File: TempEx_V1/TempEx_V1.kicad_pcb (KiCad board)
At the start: 4 copper layers, 50 x 40 mm, 29 parts, among them J1 Conn_01x02, J2 Conn_01x10, J3 Conn_01x02, J4 Conn_01x02, J5 Conn_01x02, U1 MAX31865xTP, U2 MAX31865xTP, U3 MAX31865xTP, U4 MAX31865xTP

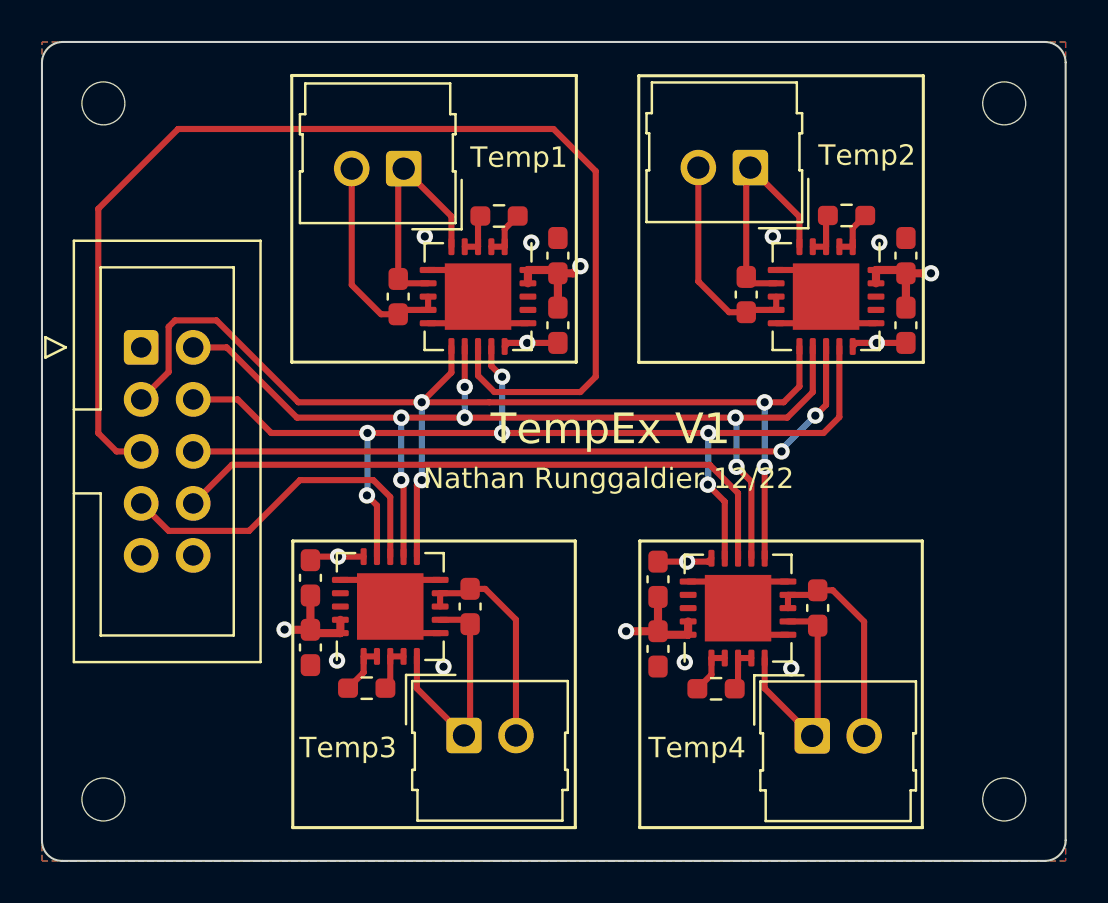
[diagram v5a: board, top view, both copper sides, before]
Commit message: Layer change + 4 pin setup + stitching
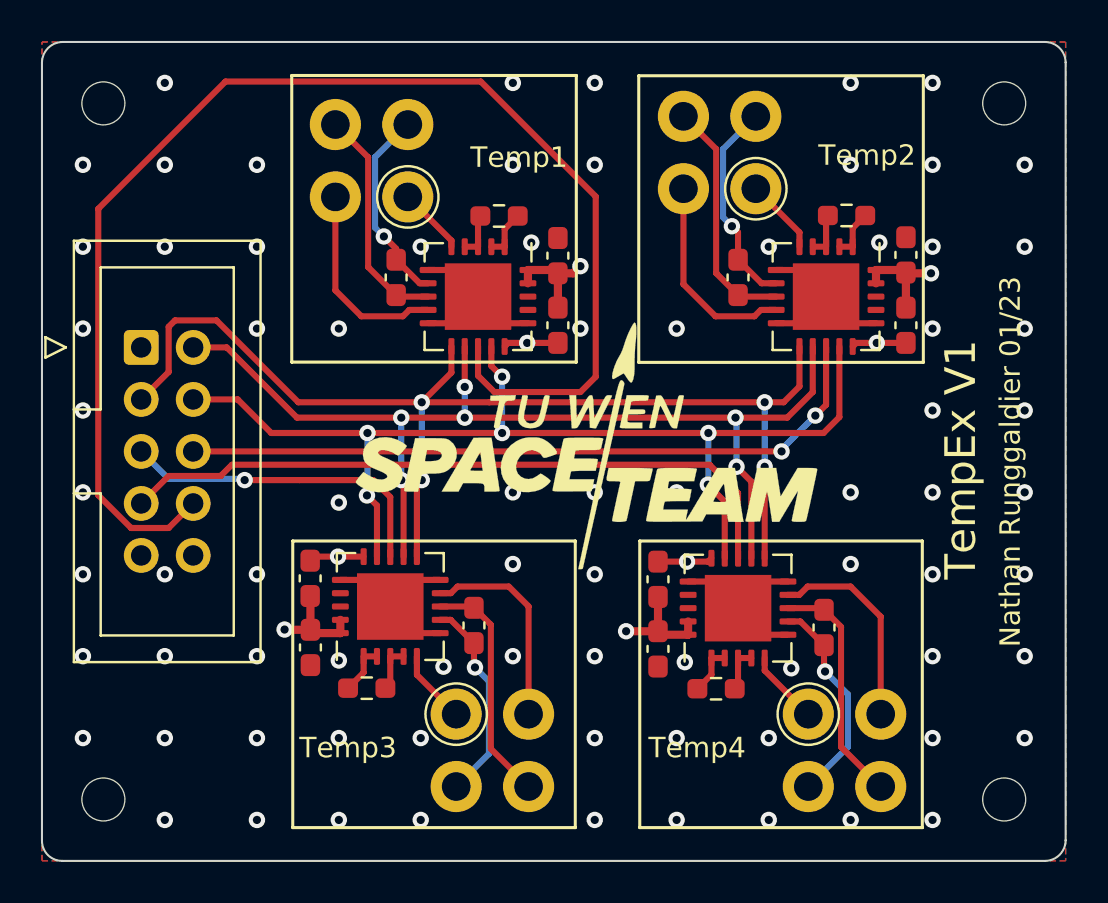
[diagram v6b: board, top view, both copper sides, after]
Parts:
- added G1: SpaceTeam_LOGO, TXV_Library_Footprints:ST_Logo_new, F.Cu at (126.6, 124.7)
- J1, J3, J4, J5: value Conn_01x02 -> Conn_01x04; footprint Connector_Molex:Molex_SL_171971-0002_1x02_P2.54mm_Vertical -> TXV_Library_Footprints:TE_M12_4_Pin_PCB
- moved C6 25.5 mm to (134.0, 116.5), turned to -90 degrees
- moved C3 24.9 mm to (117.3, 116.5), turned to -90 degrees
- moved C9 16.5 mm to (121.1, 133.5), turned to 90 degrees
- moved C10 8.04 mm to (142.2, 115.4), turned to 90 degrees
- moved C11 7.93 mm to (113.1, 131.2)
- moved J5 1.73 mm to (139.2, 139.6), turned to 90 degrees
- moved J3 1.67 mm to (133.1, 110.4), turned to -90 degrees
- moved J1 1.62 mm to (116.1, 110.8), turned to -90 degrees
- moved J4 1.57 mm to (122.0, 139.6), turned to 90 degrees
- moved C12 1.00 mm to (138.2, 133.6)
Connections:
- net /Temperature/SPI_CLK renamed /SPI_CLK
- net /Temperature/SPI_MISO renamed /SPI_MISO
- net /Temperature/SPI_MOSI renamed /SPI_MOSI
- net /Temperature/SPI_NSS2 renamed /SPI_NSS2
- C10 pad 1: Net-(C10-Pad1) -> +3V3
- C10 pad 2: Net-(C10-Pad2) -> GND
- C11 pad 1: Net-(C11-Pad1) -> +3V3
- C11 pad 2: Net-(C11-Pad2) -> GND
- C3 pad 1: +3V3 -> Net-(C3-Pad1)
- C3 pad 2: GND -> Net-(C3-Pad2)
- C6 pad 1: +3V3 -> Net-(C6-Pad1)
- C6 pad 2: GND -> Net-(C6-Pad2)
- J1 pad 1: Net-(C9-Pad1) -> Net-(J1-Pad1)
- J1 pad 2: Net-(C9-Pad2) -> Net-(C3-Pad1)
- J2 pad 5: /Temperature/SPI_NSS1 -> /SPI_NSS1
- J2 pad 7: /Temperature/SPI_NSS3 -> /SPI_NSS3
- J2 pad 8: /Temperature/SPI_NSS4 -> /SPI_NSS4
- J3 pad 1: Net-(C10-Pad1) -> Net-(J3-Pad1)
- J3 pad 2: Net-(C10-Pad2) -> Net-(C6-Pad1)
- J4 pad 1: Net-(C11-Pad1) -> Net-(J4-Pad1)
- J4 pad 2: Net-(C11-Pad2) -> Net-(C9-Pad1)
- J5 pad 1: Net-(C12-Pad1) -> Net-(J5-Pad1)
- J5 pad 2: Net-(C12-Pad2) -> Net-(C12-Pad1)
- U1 pad 13: /Temperature/SPI_NSS1 -> /SPI_NSS4
- U1 pad 5: Net-(C9-Pad1) -> Net-(J1-Pad1)
- U1 pad 7: Net-(C9-Pad1) -> Net-(C3-Pad1)
- U1 pad 8: Net-(C9-Pad2) -> Net-(C3-Pad2)
- U1 pad 9: Net-(C9-Pad2) -> Net-(J1-Pad4)
- U2 pad 5: Net-(C10-Pad1) -> Net-(J3-Pad1)
- U2 pad 7: Net-(C10-Pad1) -> Net-(C6-Pad1)
- U2 pad 8: Net-(C10-Pad2) -> Net-(C6-Pad2)
- U2 pad 9: Net-(C10-Pad2) -> Net-(J3-Pad4)
- U3 pad 13: /Temperature/SPI_NSS3 -> /SPI_NSS1
- U3 pad 5: Net-(C11-Pad1) -> Net-(J4-Pad1)
- U3 pad 7: Net-(C11-Pad1) -> Net-(C9-Pad1)
- U3 pad 8: Net-(C11-Pad2) -> Net-(C9-Pad2)
- U3 pad 9: Net-(C11-Pad2) -> Net-(J4-Pad4)
- U4 pad 13: /Temperature/SPI_NSS4 -> /SPI_NSS3
- U4 pad 5: Net-(C12-Pad1) -> Net-(J5-Pad1)
- U4 pad 9: Net-(C12-Pad2) -> Net-(J5-Pad4)
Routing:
- net /SPI_NSS4: track 0.00 -> 65.6 mm
- net /Temperature/SPI_NSS1: track 58.0 -> 0.00 mm
- net /SPI_NSS3: track 0.00 -> 33.7 mm
- net /Temperature/SPI_NSS4: track 31.1 -> 0.00 mm
- net /Temperature/SPI_NSS3: track 17.0 -> 0.00 mm
- net /SPI_NSS1: track 0.00 -> 16.0 mm, vias 0 -> 1
- net Net-(C11-Pad1): track 11.9 -> 0.00 mm
- net Net-(C10-Pad1): track 11.9 -> 0.00 mm
- net Net-(C6-Pad2): track 0.00 -> 11.7 mm
- net Net-(C3-Pad2): track 0.00 -> 11.2 mm
- net Net-(C11-Pad2): track 10.7 -> 0.00 mm
- net Net-(C10-Pad2): track 10.7 -> 0.00 mm
- net Net-(C6-Pad1): track 0.00 -> 10.3 mm, vias 0 -> 1
- net Net-(J4-Pad4): track 0.00 -> 10.1 mm
- net Net-(J5-Pad4): track 0.00 -> 10.1 mm
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- added copper zone on In2.Cu, net +3V3
- added copper zone on In1.Cu, net GND
- removed copper zone on In1.Cu, net +3V3
- removed copper zone on In2.Cu, net GND
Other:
- board text added: "Nathan Runggaldier 01/23"
- board text removed: "Nathan Runggaldier 12/22"
